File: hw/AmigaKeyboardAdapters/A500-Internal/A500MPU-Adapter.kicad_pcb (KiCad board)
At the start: 2 copper layers, 24.1 x 30.5 mm, 13 parts, among them P1 CONN_01X08, P2 CONN_01X08, P3 CONN_02X03, P4 CONN_01X02, P5 CONN_01X02

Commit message: Added new capacitors filter on the Vcc line (backside)
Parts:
- added C1: 10uF, SMD_Packages:SMD-1206_Pol, B.Cu at (148.6, 107.3)
- added C2: 100nF, Capacitors_SMD:C_1206_HandSoldering, B.Cu at (164.5, 113.7)
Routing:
- net VCC: track 36.9 -> 60.5 mm, vias 3 -> 5
- net GND: track 53.7 -> 60.3 mm, vias 2 -> 3
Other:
- board text added: "RBL006.002"
- board text removed: "RBL006.001"
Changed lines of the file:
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@@
 (kicad_pcb (version 4) (host pcbnew 4.0.2+dfsg1-stable)
   (general
-    (links 28)
+    (links 32)
     (no_connects 0)
     (area 144.704999 96.444999 168.985001 127.075001)
     (thickness 1.6)
     (drawings 10)
-    (tracks 197)
+    (tracks 216)
     (zones 0)
-    (modules 13)
+    (modules 15)
     (nets 13)
   )
@@
       (drillshape 0)
       (scaleselection 1)
-      (outputdirectory /home/debian/AMIGA/projects/AmigaKeyboardAdapters/A500-Internal/production/))
+      (outputdirectory production/))
   )
   (net 0 "")
@@
     )
   )
+  (module SMD_Packages:SMD-1206_Pol (layer B.Cu)
+    (at 148.59 107.315 270)
+    (attr smd)
+    (fp_text reference C1 (at 0 2.54 270) (layer B.SilkS)
+      (effects (font (size 1 1) (thickness 0.15)) (justify mirror))
+    )
+    (fp_text value 10uF (at 0 0 270) (layer B.Fab)
+      (effects (font (size 1 1) (thickness 0.15)) (justify mirror))
+    )
+    (fp_line (start -2.54 1.143) (end -2.794 1.143) (layer B.SilkS) (width 0.15))
+    (fp_line (start -2.794 1.143) (end -2.794 -1.143) (layer B.SilkS) (width 0.15))
+    (fp_line (start -2.794 -1.143) (end -2.54 -1.143) (layer B.SilkS) (width 0.15))
+    (fp_line (start -2.54 1.143) (end -2.54 -1.143) (layer B.SilkS) (width 0.15))
+    (fp_line (start -2.54 -1.143) (end -0.889 -1.143) (layer B.SilkS) (width 0.15))
+    (fp_line (start 0.889 1.143) (end 2.54 1.143) (layer B.SilkS) (width 0.15))
+    (fp_line (start 2.54 1.143) (end 2.54 -1.143) (layer B.SilkS) (width 0.15))
+    (fp_line (start 2.54 -1.143) (end 0.889 -1.143) (layer B.SilkS) (width 0.15))
+    (fp_line (start -0.889 1.143) (end -2.54 1.143) (layer B.SilkS) (width 0.15))
+    (pad 1 smd rect (at -1.651 0 270) (size 1.524 2.032) (layers B.Cu B.Paste B.Mask)
+      (net 8 VCC))
+    (pad 2 smd rect (at 1.651 0 270) (size 1.524 2.032) (layers B.Cu B.Paste B.Mask)
+      (net 1 GND))
+    (model SMD_Packages.3dshapes/SMD-1206_Pol.wrl
+      (at (xyz 0 0 0))
+      (scale (xyz 0.17 0.16 0.16))
+      (rotate (xyz 0 0 0))
+    )
+  )
+  (module Capacitors_SMD:C_1206_HandSoldering (layer B.Cu)
+    (at 164.465 113.665 270)
+    (descr "Capacitor SMD 1206, hand soldering")
+    (tags "capacitor 1206")
+    (attr smd)
+    (fp_text reference C2 (at 0 2.3 270) (layer B.SilkS)
+      (effects (font (size 1 1) (thickness 0.15)) (justify mirror))
+    )
+    (fp_text value 100nF (at 0 -2.3 270) (layer B.Fab)
+      (effects (font (size 1 1) (thickness 0.15)) (justify mirror))
+    )
+    (fp_line (start -3.3 1.15) (end 3.3 1.15) (layer B.CrtYd) (width 0.05))
+    (fp_line (start -3.3 -1.15) (end 3.3 -1.15) (layer B.CrtYd) (width 0.05))
+    (fp_line (start -3.3 1.15) (end -3.3 -1.15) (layer B.CrtYd) (width 0.05))
+    (fp_line (start 3.3 1.15) (end 3.3 -1.15) (layer B.CrtYd) (width 0.05))
+    (fp_line (start 1 1.025) (end -1 1.025) (layer B.SilkS) (width 0.15))
+    (fp_line (start -1 -1.025) (end 1 -1.025) (layer B.SilkS) (width 0.15))
+    (pad 1 smd rect (at -2 0 270) (size 2 1.6) (layers B.Cu B.Paste B.Mask)
+      (net 8 VCC))
+    (pad 2 smd rect (at 2 0 270) (size 2 1.6) (layers B.Cu B.Paste B.Mask)
+      (net 1 GND))
+    (model Capacitors_SMD.3dshapes/C_1206_HandSoldering.wrl
+      (at (xyz 0 0 0))
+      (scale (xyz 1 1 1))
+      (rotate (xyz 0 0 0))
+    )
+  )
   (dimension 30.48 (width 0.3) (layer Margin)
     (gr_text "30,480 mm" (at 174.578 111.76 270) (layer Margin)
@@
     (effects (font (size 0.7 1) (thickness 0.17)))
   )
-  (gr_text "in memoriam A.S.-G.D." (at 146.05 107.315 90) (layer B.SilkS)
+  (gr_text "in memoriam A.S.-G.D." (at 145.415 116.205 90) (layer B.SilkS)
     (effects (font (size 0.5 0.7) (thickness 0.1)))
   )
@@
     (effects (font (size 0.5 0.7) (thickness 0.1)))
   )
-  (gr_text RBL006.001 (at 157.48 121.92) (layer B.SilkS)
+  (gr_text RBL006.002 (at 157.48 121.92) (layer B.SilkS)
     (effects (font (size 1.5 1.5) (thickness 0.3)))
   )
@@
   (gr_line (start 144.78 127) (end 168.91 127) (angle 90) (layer Edge.Cuts) (width 0.15))
   (gr_line (start 144.78 96.52) (end 144.78 127) (angle 90) (layer Edge.Cuts) (width 0.15))
+  (segment (start 148.59 109.601) (end 146.939 109.601) (width 0.25) (layer B.Cu) (net 1))
+  (via (at 146.685 109.855) (size 0.6) (drill 0.4) (layers F.Cu B.Cu) (net 1))
+  (segment (start 146.939 109.601) (end 146.685 109.855) (width 0.25) (layer B.Cu) (net 1))
+  (segment (start 164.465 115.665) (end 164.37 115.665) (width 0.25) (layer B.Cu) (net 1))
+  (segment (start 164.37 115.665) (end 162.56 117.475) (width 0.25) (layer B.Cu) (net 1))
+  (segment (start 162.56 117.475) (end 162.56 119.38) (width 0.25) (layer B.Cu) (net 1))
   (segment (start 158.258 102.87) (end 158.258 104.029) (width 0.25) (layer F.Cu) (net 1))
   (segment (start 158.877 109.982) (end 157.48 111.379) (width 0.25) (layer B.Cu) (net 1))
@@
   (segment (start 153.67 118.872) (end 153.67 123.19) (width 0.25) (layer B.Cu) (net 7))
   (segment (start 154.94 117.602) (end 153.67 118.872) (width 0.25) (layer B.Cu) (net 7))
+  (segment (start 148.59 106.299) (end 148.59 106.045) (width 0.25) (layer B.Cu) (net 8))
+  (segment (start 148.59 106.045) (end 149.86 104.775) (width 0.25) (layer B.Cu) (net 8))
+  (segment (start 149.86 104.775) (end 151.638 104.775) (width 0.25) (layer B.Cu) (net 8))
+  (segment (start 151.638 104.775) (end 152.908 103.505) (width 0.25) (layer B.Cu) (net 8))
+  (segment (start 164.465 111.665) (end 164.465 108.585) (width 0.25) (layer B.Cu) (net 8))
+  (segment (start 156.591 105.791) (end 156.591 107.442) (width 0.25) (layer B.Cu) (net 8))
+  (segment (start 156.21 105.41) (end 156.591 105.791) (width 0.25) (layer B.Cu) (net 8))
+  (segment (start 156.21 104.775) (end 156.21 105.41) (width 0.25) (layer B.Cu) (net 8))
+  (segment (start 160.655 104.775) (end 156.21 104.775) (width 0.25) (layer B.Cu) (net 8))
+  (via (at 160.655 104.775) (size 0.6) (drill 0.4) (layers F.Cu B.Cu) (net 8))
+  (segment (start 164.465 104.775) (end 160.655 104.775) (width 0.25) (layer F.Cu) (net 8))
+  (segment (start 164.465 108.585) (end 164.465 104.775) (width 0.25) (layer F.Cu) (net 8))
+  (via (at 164.465 108.585) (size 0.6) (drill 0.4) (layers F.Cu B.Cu) (net 8))
   (segment (start 150.908 102.87) (end 152.781 102.87) (width 0.25) (layer F.Cu) (net 8))
   (segment (start 159.258 113.157) (end 158.115 114.3) (width 0.25) (layer B.Cu) (net 8))
@@
     (polygon
       (pts
-        (xy 168.402 126.746) (xy 145.288 126.746) (xy 145.288 97.028) (xy 168.402 97.028) (xy 168.402 126.746)
+        (xy 168.275 126.365) (xy 145.415 126.365) (xy 145.415 97.155) (xy 168.275 97.155) (xy 168.275 126.365)
       )
     )

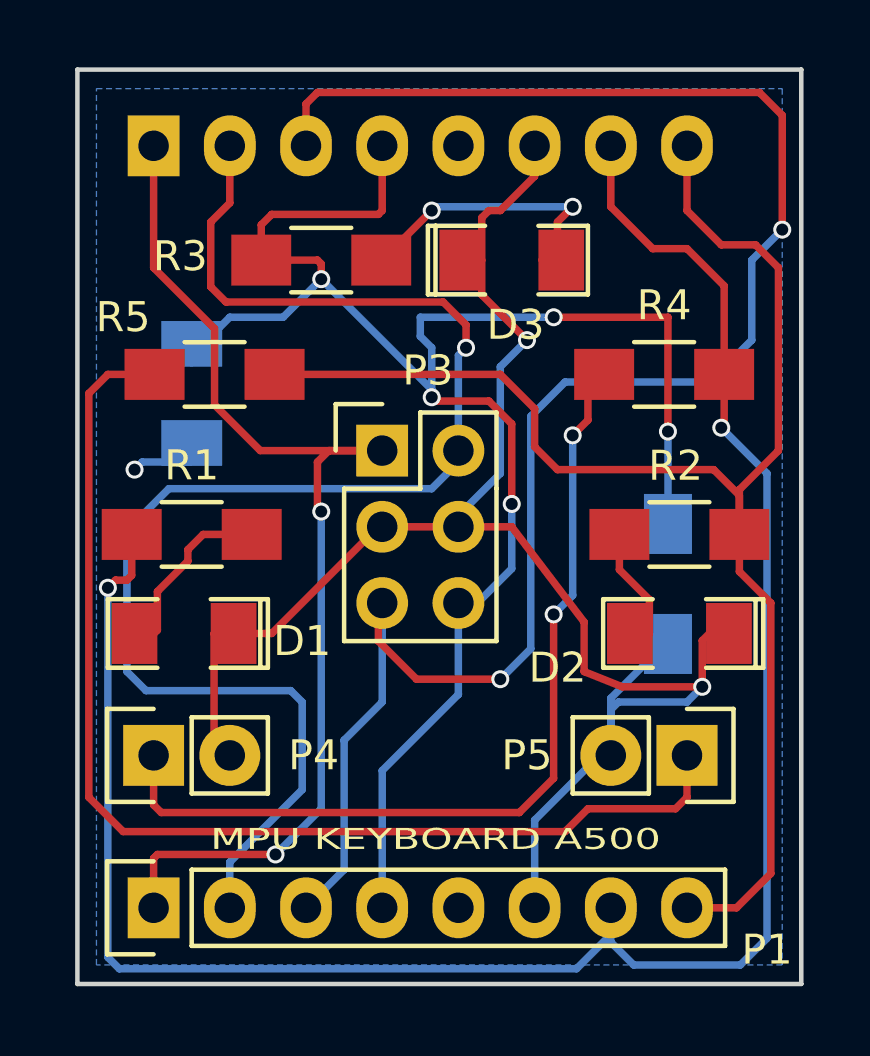
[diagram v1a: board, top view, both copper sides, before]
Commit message: added the idc 2x3 box
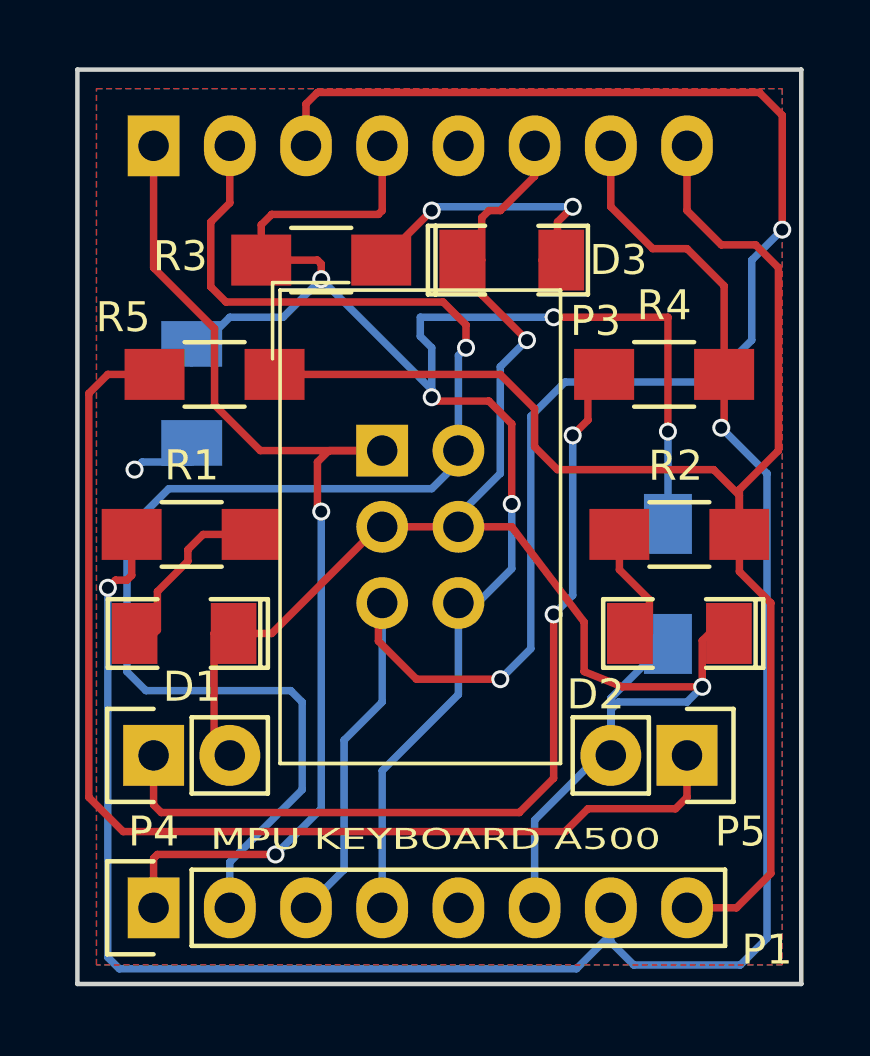
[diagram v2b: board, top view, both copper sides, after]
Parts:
- P3: footprint Pin_Headers:Pin_Header_Straight_2x03 -> RetroBitLab:IDC-Header_2x03_P2.54mm_Vertical
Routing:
- added copper zone on F.Cu, net GND
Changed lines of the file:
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@@
     (links 32)
     (no_connects 0)
-    (area 144.704999 96.444999 168.985001 127.075001)
+    (area 144.704999 90.876 181.228 127.075001)
     (thickness 1.6)
     (drawings 10)
@@
     )
   )
-  (module Pin_Headers:Pin_Header_Straight_2x03 (layer F.Cu)
-    (at 154.94 109.22)
-    (descr "Through hole pin header")
-    (tags "pin header")
-    (fp_text reference P3 (at 1.524 -2.667) (layer F.SilkS)
-      (effects (font (size 1 1) (thickness 0.15)))
-    )
-    (fp_text value CONN_02X03 (at 0 -3.1) (layer F.Fab)
-      (effects (font (size 1 1) (thickness 0.15)))
-    )
-    (fp_line (start -1.27 1.27) (end -1.27 6.35) (layer F.SilkS) (width 0.15))
-    (fp_line (start -1.55 -1.55) (end 0 -1.55) (layer F.SilkS) (width 0.15))
-    (fp_line (start -1.75 -1.75) (end -1.75 6.85) (layer F.CrtYd) (width 0.05))
-    (fp_line (start 4.3 -1.75) (end 4.3 6.85) (layer F.CrtYd) (width 0.05))
-    (fp_line (start -1.75 -1.75) (end 4.3 -1.75) (layer F.CrtYd) (width 0.05))
-    (fp_line (start -1.75 6.85) (end 4.3 6.85) (layer F.CrtYd) (width 0.05))
-    (fp_line (start 1.27 -1.27) (end 1.27 1.27) (layer F.SilkS) (width 0.15))
-    (fp_line (start 1.27 1.27) (end -1.27 1.27) (layer F.SilkS) (width 0.15))
-    (fp_line (start -1.27 6.35) (end 3.81 6.35) (layer F.SilkS) (width 0.15))
-    (fp_line (start 3.81 6.35) (end 3.81 1.27) (layer F.SilkS) (width 0.15))
-    (fp_line (start -1.55 -1.55) (end -1.55 0) (layer F.SilkS) (width 0.15))
-    (fp_line (start 3.81 -1.27) (end 1.27 -1.27) (layer F.SilkS) (width 0.15))
-    (fp_line (start 3.81 1.27) (end 3.81 -1.27) (layer F.SilkS) (width 0.15))
-    (pad 1 thru_hole rect (at 0 0) (size 1.7272 1.7272) (drill 1.016) (layers *.Cu *.Mask F.SilkS)
-      (net 5 CLOCK))
-    (pad 2 thru_hole oval (at 2.54 0) (size 1.7272 1.7272) (drill 1.016) (layers *.Cu *.Mask F.SilkS)
-      (net 6 DATA))
-    (pad 3 thru_hole oval (at 0 2.54) (size 1.7272 1.7272) (drill 1.016) (layers *.Cu *.Mask F.SilkS)
-      (net 1 GND))
-    (pad 4 thru_hole oval (at 2.54 2.54) (size 1.7272 1.7272) (drill 1.016) (layers *.Cu *.Mask F.SilkS)
-      (net 1 GND))
-    (pad 5 thru_hole oval (at 0 5.08) (size 1.7272 1.7272) (drill 1.016) (layers *.Cu *.Mask F.SilkS)
-      (net 7 RESET))
-    (pad 6 thru_hole oval (at 2.54 5.08) (size 1.7272 1.7272) (drill 1.016) (layers *.Cu *.Mask F.SilkS)
-      (net 8 VCC))
-    (model Pin_Headers.3dshapes/Pin_Header_Straight_2x03.wrl
-      (at (xyz 0.05 -0.1 0))
-      (scale (xyz 1 1 1))
-      (rotate (xyz 0 0 90))
-    )
-  )
   (module Resistors_SMD:R_1206_HandSoldering (layer F.Cu)
     (at 149.352 106.68)
@@
     (descr "Through hole pin header")
     (tags "pin header")
-    (fp_text reference P5 (at 0 5.334 360) (layer F.SilkS)
+    (fp_text reference P5 (at 2.54 -1.778 360) (layer F.SilkS)
       (effects (font (size 1 1) (thickness 0.15)))
     )
@@
     (descr "Through hole pin header")
     (tags "pin header")
-    (fp_text reference P4 (at 0 5.334 180) (layer F.SilkS)
+    (fp_text reference P4 (at -2.54 0 180) (layer F.SilkS)
       (effects (font (size 1 1) (thickness 0.15)))
     )
@@
     (at 159.258 102.87)
     (attr smd)
-    (fp_text reference D3 (at 0.127 2.159) (layer F.SilkS)
+    (fp_text reference D3 (at 3.556 0) (layer F.SilkS)
       (effects (font (size 1 1) (thickness 0.15)))
     )
@@
     (at 164.846 115.316 180)
     (attr smd)
-    (fp_text reference D2 (at 4.064 -1.143 180) (layer F.SilkS)
+    (fp_text reference D2 (at 2.794 -2.032 180) (layer F.SilkS)
       (effects (font (size 1 1) (thickness 0.15)))
     )
@@
     (at 148.336 115.316 180)
     (attr smd)
-    (fp_text reference D1 (at -3.937 -0.254 180) (layer F.SilkS)
+    (fp_text reference D1 (at -0.254 -1.778 180) (layer F.SilkS)
       (effects (font (size 1 1) (thickness 0.15)))
     )
@@
       (net 1 GND))
     (model Capacitors_SMD.3dshapes/C_1206_HandSoldering.wrl
+      (at (xyz 0 0 0))
+      (scale (xyz 1 1 1))
+      (rotate (xyz 0 0 0))
+    )
+  )
+  (module RetroBitLab:IDC-Header_2x03_P2.54mm_Vertical (layer F.Cu)
+    (at 154.94 109.22)
+    (descr "Through hole straight IDC box header, 2x03, 2.54mm pitch, double rows")
+    (tags "Through hole IDC box header THT 2x03 2.54mm double row")
+    (fp_text reference P3 (at 7.112 -4.318) (layer F.SilkS)
+      (effects (font (size 1 1) (thickness 0.15)))
+    )
+    (fp_text value CONN_02X03 (at 1.27 11.684) (layer F.Fab)
+      (effects (font (size 1 1) (thickness 0.15)))
+    )
+    (fp_text user %R (at 1.27 2.54) (layer F.Fab)
+      (effects (font (size 1 1) (thickness 0.15)))
+    )
+    (fp_line (start 5.695 -5.1) (end 5.695 10.18) (layer F.Fab) (width 0.1))
+    (fp_line (start 5.145 -4.56) (end 5.145 9.62) (layer F.Fab) (width 0.1))
+    (fp_line (start -3.155 -5.1) (end -3.155 10.18) (layer F.Fab) (width 0.1))
+    (fp_line (start -2.605 -4.56) (end -2.605 0.29) (layer F.Fab) (width 0.1))
+    (fp_line (start -2.605 4.79) (end -2.605 9.62) (layer F.Fab) (width 0.1))
+    (fp_line (start -2.605 0.29) (end -3.155 0.29) (layer F.Fab) (width 0.1))
+    (fp_line (start -2.605 4.79) (end -3.155 4.79) (layer F.Fab) (width 0.1))
+    (fp_line (start 5.695 -5.1) (end -3.155 -5.1) (layer F.Fab) (width 0.1))
+    (fp_line (start 5.145 -4.56) (end -2.605 -4.56) (layer F.Fab) (width 0.1))
+    (fp_line (start 5.695 10.18) (end -3.155 10.18) (layer F.Fab) (width 0.1))
+    (fp_line (start 5.145 9.62) (end -2.605 9.62) (layer F.Fab) (width 0.1))
+    (fp_line (start 5.695 -5.1) (end 5.145 -4.56) (layer F.Fab) (width 0.1))
+    (fp_line (start 5.695 10.18) (end 5.145 9.62) (layer F.Fab) (width 0.1))
+    (fp_line (start -3.155 -5.1) (end -2.605 -4.56) (layer F.Fab) (width 0.1))
+    (fp_line (start -3.155 10.18) (end -2.605 9.62) (layer F.Fab) (width 0.1))
+    (fp_line (start 5.95 -5.35) (end 5.95 10.43) (layer F.CrtYd) (width 0.05))
+    (fp_line (start 5.95 10.43) (end -3.41 10.43) (layer F.CrtYd) (width 0.05))
+    (fp_line (start -3.41 10.43) (end -3.41 -5.35) (layer F.CrtYd) (width 0.05))
+    (fp_line (start -3.41 -5.35) (end 5.95 -5.35) (layer F.CrtYd) (width 0.05))
+    (fp_line (start 5.945 -5.35) (end 5.945 10.43) (layer F.SilkS) (width 0.12))
+    (fp_line (start 5.945 10.43) (end -3.405 10.43) (layer F.SilkS) (width 0.12))
+    (fp_line (start -3.405 10.43) (end -3.405 -5.35) (layer F.SilkS) (width 0.12))
+    (fp_line (start -3.405 -5.35) (end 5.945 -5.35) (layer F.SilkS) (width 0.12))
+    (fp_line (start -3.655 -5.6) (end -3.655 -3.06) (layer F.SilkS) (width 0.12))
+    (fp_line (start -3.655 -5.6) (end -1.115 -5.6) (layer F.SilkS) (width 0.12))
+    (pad 1 thru_hole rect (at 0 0) (size 1.7272 1.7272) (drill 1.016) (layers *.Cu *.Mask)
+      (net 5 CLOCK))
+    (pad 2 thru_hole oval (at 2.54 0) (size 1.7272 1.7272) (drill 1.016) (layers *.Cu *.Mask)
+      (net 6 DATA))
+    (pad 3 thru_hole oval (at 0 2.54) (size 1.7272 1.7272) (drill 1.016) (layers *.Cu *.Mask)
+      (net 1 GND))
+    (pad 4 thru_hole oval (at 2.54 2.54) (size 1.7272 1.7272) (drill 1.016) (layers *.Cu *.Mask)
+      (net 1 GND))
+    (pad 5 thru_hole oval (at 0 5.08) (size 1.7272 1.7272) (drill 1.016) (layers *.Cu *.Mask)
+      (net 7 RESET))
+    (pad 6 thru_hole oval (at 2.54 5.08) (size 1.7272 1.7272) (drill 1.016) (layers *.Cu *.Mask)
+      (net 8 VCC))
+    (model /home/debian/packages/kicad/kicad-packages3D/Connector_IDC.3dshapes/IDC-Header_2x03_P2.54mm_Vertical.wrl
       (at (xyz 0 0 0))
       (scale (xyz 1 1 1))
@@
     (connect_pads (clearance 0.508))
     (min_thickness 0.254)
+    (fill yes (arc_segments 16) (thermal_gap 0.508) (thermal_bridge_width 0.508))
+    (polygon
+      (pts
+        (xy 168.275 126.365) (xy 145.415 126.365) (xy 145.415 97.155) (xy 168.275 97.155) (xy 168.275 126.365)
+      )
+    )
+  )
+  (zone (net 1) (net_name GND) (layer F.Cu) (hatch edge 0.508)
+    (connect_pads (clearance 0.508))
+    (min_thickness 0.254)

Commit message: From KiCAD 4 to KiCAD 5
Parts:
- C1: footprint SMD_Packages:SMD-1206_Pol -> Capacitor_Tantalum_SMD:CP_EIA-3216-12_Kemet-S_Pad1.58x1.35mm_HandSolder; moved to F.Cu
- C2: footprint Capacitors_SMD:C_1206_HandSoldering -> Capacitor_SMD:C_1206_3216Metric_Pad1.33x1.80mm_HandSolder; moved to F.Cu
- D1: value LED GREEN -> POWER ORANGE; footprint SMD_Packages:SMD-1206_Pol -> LED_SMD:LED_1206_3216Metric_Pad1.42x1.75mm_HandSolder
- D2: value DISK YELLOW -> FLOPPY GREEN; footprint SMD_Packages:SMD-1206_Pol -> LED_SMD:LED_1206_3216Metric_Pad1.42x1.75mm_HandSolder
- D3: footprint SMD_Packages:SMD-1206_Pol -> LED_SMD:LED_1206_3216Metric_Pad1.42x1.75mm_HandSolder
- P1: value CONN_01X08 -> Conn_01x08; footprint Pin_Headers:Pin_Header_Straight_1x08 -> Connector_PinHeader_2.54mm:PinHeader_1x08_P2.54mm_Vertical
- P2: value CONN_01X08 -> Conn_01x08; footprint Socket_Strips:Socket_Strip_Straight_1x08 -> Connector_PinSocket_2.54mm:PinSocket_1x08_P2.54mm_Vertical
- P3: value CONN_02X03 -> Conn_02x03; footprint RetroBitLab:IDC-Header_2x03_P2.54mm_Vertical -> Connector_IDC:IDC-Header_2x03_P2.54mm_Vertical
- P4, P5: value CONN_01X02 -> Conn_01x02; footprint Pin_Headers:Pin_Header_Straight_1x02 -> Connector_PinHeader_2.54mm:PinHeader_1x02_P2.54mm_Vertical
- R1, R2, R3, R4, R5: value 330 -> 330R; footprint Resistors_SMD:R_1206_HandSoldering -> Resistor_SMD:R_1206_3216Metric_Pad1.30x1.75mm_HandSolder
- moved D1 20.9 mm to (165.3, 103.1), turned to 0 degrees
- moved D3 20.0 mm to (148.0, 119.4)
- moved C1 18.8 mm to (164.9, 116.8), turned to 180 degrees
- moved R1 17.9 mm to (165.3, 105.6)
- moved P5 17.0 mm to (149.3, 113.2)
- moved R4 16.7 mm to (148.0, 103.3)
- moved R3 14.6 mm to (148.1, 116.7)
- moved P4 12.9 mm to (149.3, 106.6), turned to 270 degrees
- moved D2 7.02 mm to (165.2, 108.3), turned to 0 degrees
- moved R5 3.60 mm to (147.9, 110.0)
- moved P3 1.21 mm to (155.4, 108.1)
- moved R2 1.17 mm to (165.2, 110.9), turned to 0 degrees
- moved P2 0.86 mm to (148.1, 98.7), turned to 270 degrees
- moved P1 0.79 mm to (148.1, 124.6)
- moved C2 0.73 mm to (165.0, 114.2), turned to 180 degrees
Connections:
- C1 pad 1: VCC -> INUSE
- C2 pad 1: VCC -> INUSE
- P1 pad 4: VCC -> INUSE
- P1 pad 5: (no net) -> Net-(P1-Pad5)
- P2 pad 4: VCC -> INUSE
- P2 pad 5: (no net) -> Net-(P2-Pad5)
- P3 pad 6: VCC -> INUSE
- R3 pad 1: VCC -> INUSE
- R4 pad 1: Net-(P4-Pad1) -> STATUS
- R4 pad 2: STATUS -> Net-(P4-Pad1)
- R5 pad 1: Net-(P5-Pad1) -> INUSE
- R5 pad 2: INUSE -> Net-(P5-Pad1)
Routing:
- net VCC: track 60.5 -> 0.00 mm, vias 5 -> 0
- net INUSE: track 49.6 -> 92.3 mm
- net Net-(P5-Pad1): track 38.2 -> 3.28 mm
- net RESET: track 60.4 -> 32.2 mm, vias 2 -> 0
- net Net-(P4-Pad1): track 29.7 -> 3.40 mm, vias 2 -> 0
- net STATUS: track 69.3 -> 50.4 mm, vias 2 -> 0
- net DATA: track 49.5 -> 31.9 mm, vias 1 -> 0
- net GND: track 60.3 -> 69.6 mm, vias 3 -> 0
- net Net-(D3-Pad2): track 9.32 -> 2.77 mm, vias 2 -> 0
- net CLOCK: track 37.5 -> 32.2 mm, vias 2 -> 0
- net Net-(D1-Pad2): track 5.60 -> 2.53 mm
- net Net-(D2-Pad2): track 3.72 -> 2.63 mm
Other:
- rule pad_to_mask_clearance: 0.2 -> 0
- board text added: "designed by R.G.2018/2022"
- board text removed: "designed by R.G.2018"
